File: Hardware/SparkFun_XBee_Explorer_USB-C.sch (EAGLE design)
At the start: 54 parts, among them J3 USB Female Type C Connector, J4 QWIIC_RIGHT_ANGLE, U2 AP63203, U5 ESD Diode, U7 FT231XS

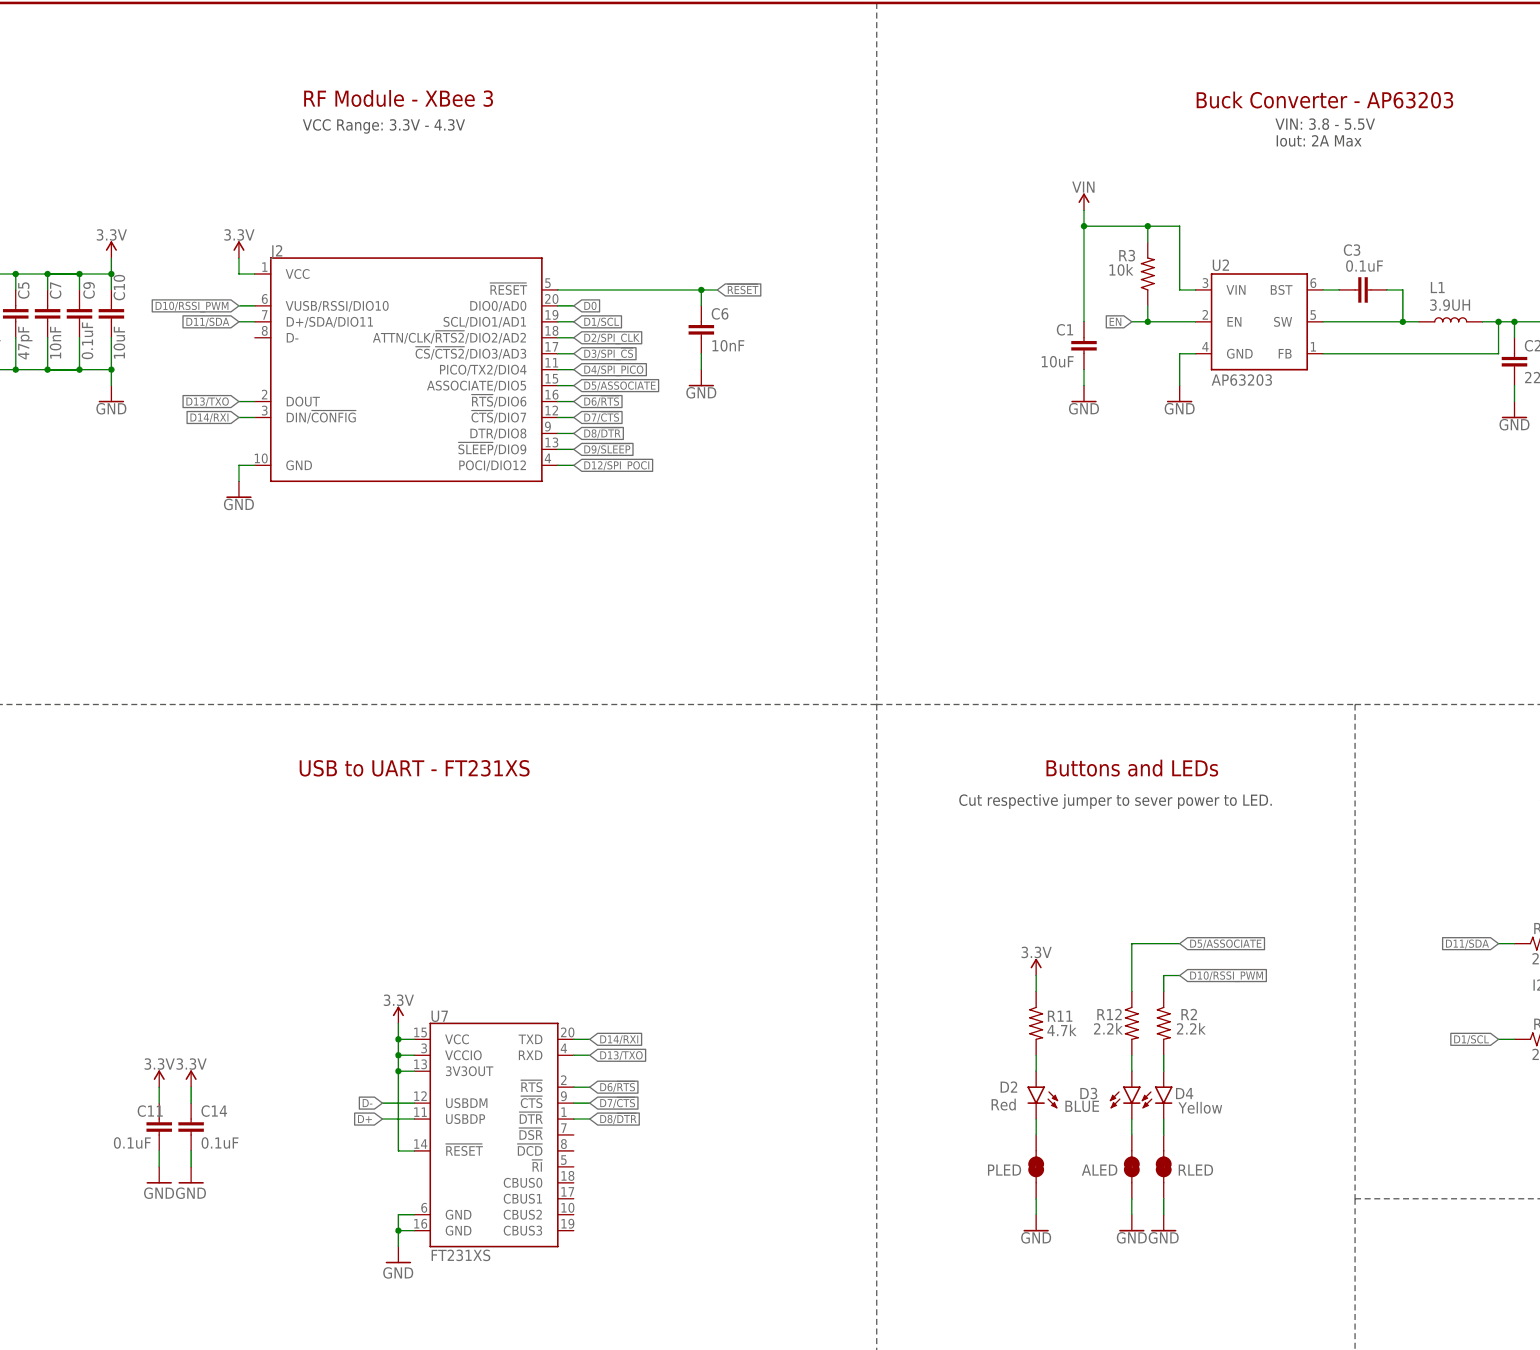
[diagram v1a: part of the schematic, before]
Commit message: Fixes anchors on some title labels in the schematic, adds more vias
* Increases the size of the Qwiic logo
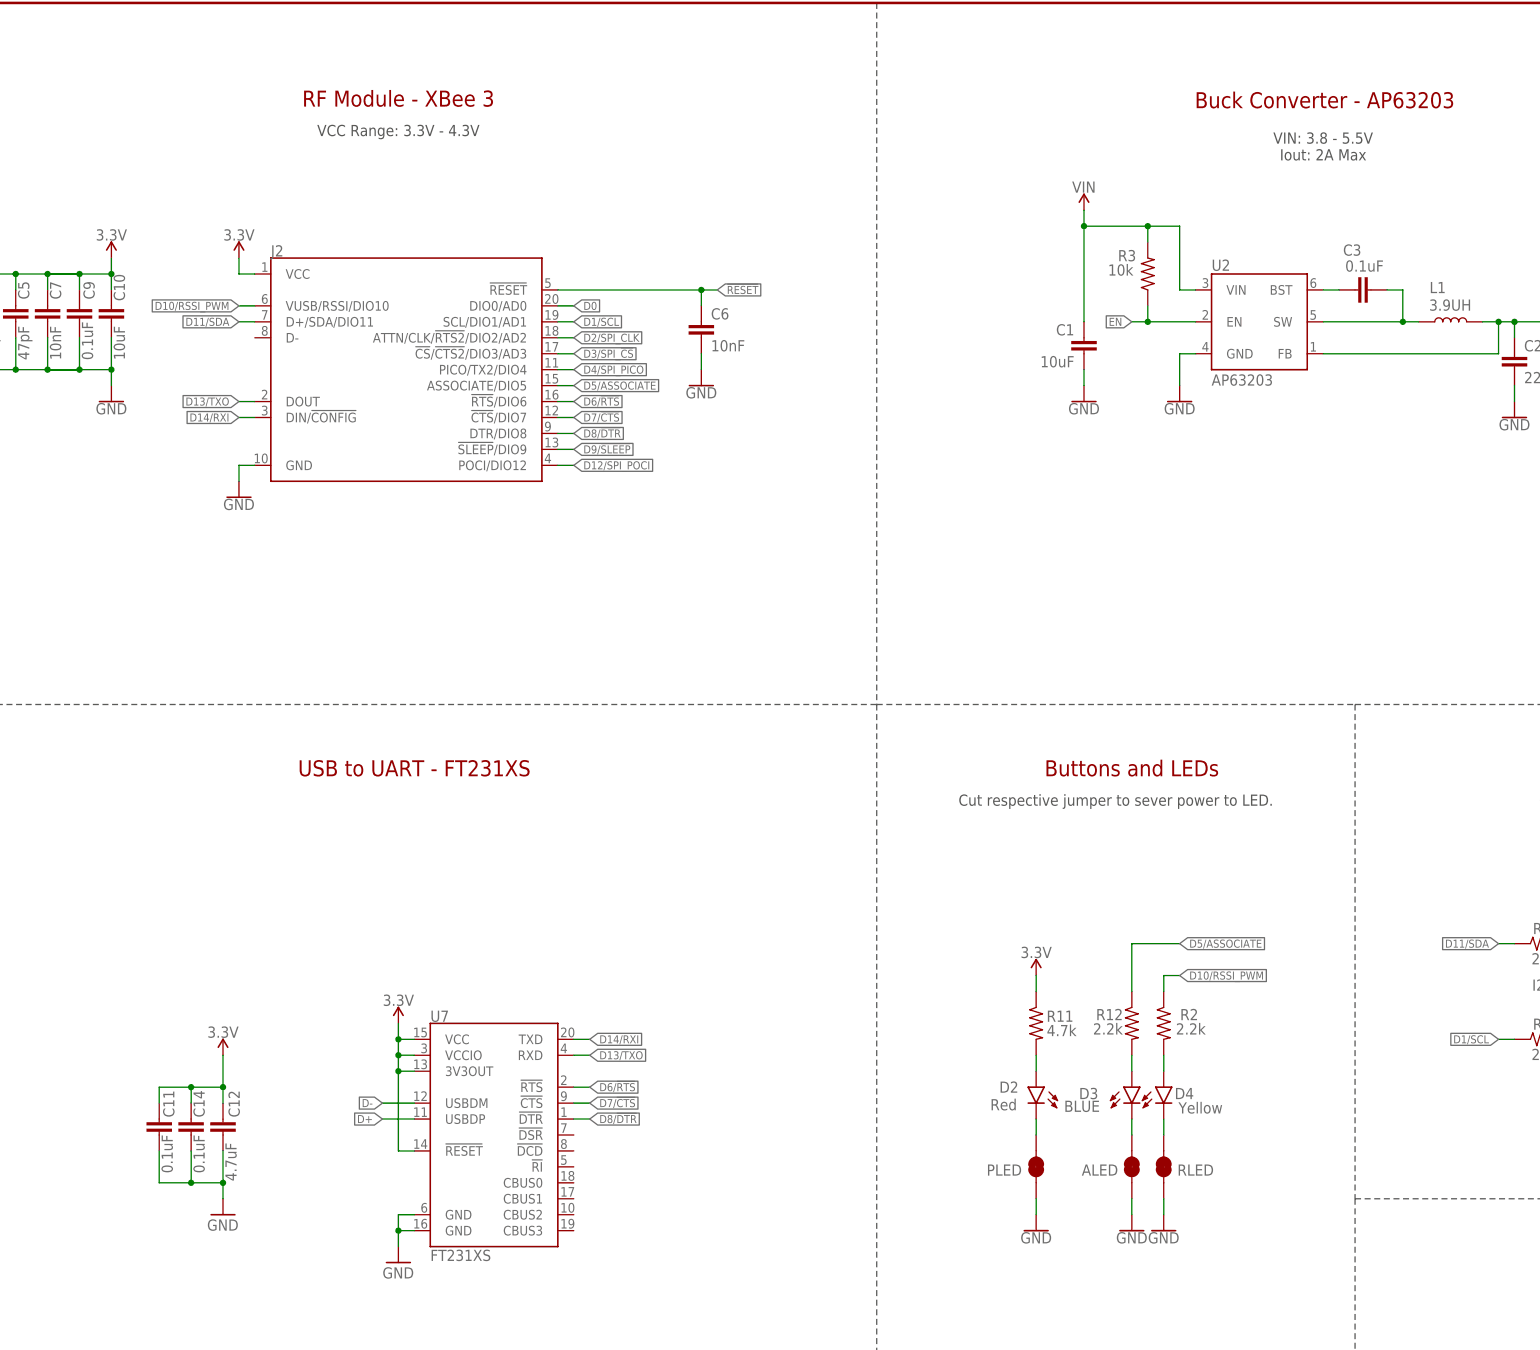
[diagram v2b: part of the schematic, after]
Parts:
- added C12: 4.7uF, SparkFun-Capacitors:4.7UF-0603-6.3V-(10%)
- LOGO3: value QWIIC_LOGO_3MM -> QWIIC_LOGO_4MM; device SparkFun-Aesthetics:QWIIC_LOGO_3MM -> SparkFun-Aesthetics:QWIIC_LOGO_4MM
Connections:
- net 3.3V: now also C12.1
- net GND: now also C12.2
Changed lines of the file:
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@@
 <part name="ALED" library="SparkFun-Jumpers" deviceset="JUMPER-SMT_2_NC_TRACE" device="_SILK" package3d_urn="urn:adsk.eagle:package:39281/1"/>
 <part name="LOGO2" library="SparkFun-Aesthetics" deviceset="OSHW-LOGO" device="S"/>
-<part name="LOGO3" library="SparkFun-Aesthetics" deviceset="QWIIC_LOGO" device="_3MM" value="QWIIC_LOGO_3MM"/>
+<part name="LOGO3" library="SparkFun-Aesthetics" deviceset="QWIIC_LOGO" device="_4MM" value="QWIIC_LOGO_4MM"/>
 <part name="U2" library="SparkFun-IC-Power" deviceset="AP63203" device="" value="AP63203"/>
 <part name="L1" library="SparkFun-Coils" deviceset="3.9UH" device="" value="3.9UH"/>
@@
 <part name="C14" library="SparkFun-Capacitors" deviceset="0.1UF" device="-0603-25V-(+80/-20%)" value="0.1uF"/>
 <part name="C11" library="SparkFun-Capacitors" deviceset="0.1UF" device="-0603-25V-(+80/-20%)" value="0.1uF"/>
-<part name="GND5" library="SparkFun-PowerSymbols" deviceset="GND" device=""/>
-<part name="SUPPLY6" library="SparkFun-PowerSymbols" deviceset="3.3V" device=""/>
-<part name="SUPPLY2" library="SparkFun-PowerSymbols" deviceset="3.3V" device=""/>
-<part name="GND8" library="SparkFun-PowerSymbols" deviceset="GND" device=""/>
 <part name="SUPPLY3" library="SparkFun-PowerSymbols" deviceset="3.3V" device=""/>
 <part name="C5" library="SparkFun-Capacitors" deviceset="47PF" device="-0603-50V-5%" value="47pF"/>
@@
 <part name="LOGO1" library="SparkFun-Aesthetics" deviceset="SFE_LOGO_NAME" device=".2_INCH"/>
 <part name="LOGO4" library="SparkFun-Aesthetics" deviceset="SPECIAL_INSTRUCTIONS" device="-ORDERING"/>
+<part name="C12" library="SparkFun-Capacitors" deviceset="4.7UF" device="-0603-6.3V-(10%)" value="4.7uF"/>
+<part name="SUPPLY12" library="SparkFun-PowerSymbols" deviceset="3.3V" device=""/>
+<part name="GND9" library="SparkFun-PowerSymbols" deviceset="GND" device=""/>
 </parts>
 <sheets>
 <sheet>
 <plain>
-<text x="60.96" y="259.08" size="1.778" layer="97" font="vector">VCC Range: 3.3V - 4.3V</text>
+<text x="76.2" y="259.08" size="1.778" layer="97" font="vector" align="center">VCC Range: 3.3V - 4.3V</text>
 <text x="223.774" y="263.906" size="2.54" layer="94" font="vector" align="center">Buck Converter - AP63203</text>
 <text x="276.86" y="157.48" size="2.54" layer="94" font="vector" align="center">Qwiic - I2C</text>
@@
 <text x="363.22" y="10.16" size="2.54" layer="94" font="vector" align="center">Elias Santistevan</text>
 <text x="193.04" y="157.48" size="2.54" layer="94" font="vector" align="center">Buttons and LEDs</text>
-<text x="215.9" y="256.54" size="1.778" layer="97" font="vector">VIN: 3.8 - 5.5V
+<text x="223.52" y="256.54" size="1.778" layer="97" font="vector" align="center">VIN: 3.8 - 5.5V
 Iout: 2A Max</text>
 <text x="276.86" y="152.4" size="1.778" layer="97" font="vector" align="center">Cut I2C jumper to remove pullups.</text>
@@
 </instance>
 <instance part="C14" gate="G$1" x="43.18" y="99.06" smashed="yes">
-<attribute name="NAME" x="44.704" y="101.981" size="1.778" layer="95" font="vector"/>
-<attribute name="VALUE" x="44.704" y="96.901" size="1.778" layer="96" font="vector"/>
+<attribute name="NAME" x="45.339" y="101.854" size="1.778" layer="95" font="vector" rot="R90"/>
+<attribute name="VALUE" x="45.339" y="92.964" size="1.778" layer="96" font="vector" rot="R90"/>
 </instance>
 <instance part="C11" gate="G$1" x="38.1" y="99.06" smashed="yes">
-<attribute name="NAME" x="34.544" y="101.981" size="1.778" layer="95" font="vector"/>
-<attribute name="VALUE" x="30.734" y="96.901" size="1.778" layer="96" font="vector"/>
-</instance>
-<instance part="GND5" gate="1" x="38.1" y="91.44" smashed="yes">
-<attribute name="VALUE" x="35.56" y="88.9" size="1.778" layer="96" font="vector"/>
-</instance>
-<instance part="SUPPLY6" gate="G$1" x="38.1" y="106.68" smashed="yes">
-<attribute name="VALUE" x="38.1" y="109.474" size="1.778" layer="96" font="vector" align="bottom-center"/>
-</instance>
-<instance part="SUPPLY2" gate="G$1" x="43.18" y="106.68" smashed="yes">
-<attribute name="VALUE" x="43.18" y="109.474" size="1.778" layer="96" font="vector" align="bottom-center"/>
-</instance>
-<instance part="GND8" gate="1" x="43.18" y="91.44" smashed="yes">
-<attribute name="VALUE" x="40.64" y="88.9" size="1.778" layer="96" font="vector"/>
+<attribute name="NAME" x="40.513" y="101.854" size="1.778" layer="95" font="vector" rot="R90"/>
+<attribute name="VALUE" x="40.259" y="92.964" size="1.778" layer="96" font="vector" rot="R90"/>
 </instance>
 <instance part="SUPPLY3" gate="G$1" x="76.2" y="116.84" smashed="yes">
@@
 <instance part="LOGO1" gate="G$1" x="330.2" y="33.02" smashed="yes"/>
 <instance part="LOGO4" gate="G$1" x="394.97" y="12.446" smashed="yes"/>
+<instance part="C12" gate="G$1" x="48.26" y="99.06" smashed="yes">
+<attribute name="NAME" x="50.927" y="101.854" size="1.778" layer="95" font="vector" rot="R90"/>
+<attribute name="VALUE" x="50.419" y="91.694" size="1.778" layer="96" font="vector" rot="R90"/>
+</instance>
+<instance part="SUPPLY12" gate="G$1" x="48.26" y="111.76" smashed="yes">
+<attribute name="VALUE" x="48.26" y="114.554" size="1.778" layer="96" font="vector" align="bottom-center"/>
+</instance>
+<instance part="GND9" gate="1" x="48.26" y="86.36" smashed="yes">
+<attribute name="VALUE" x="45.72" y="83.82" size="1.778" layer="96" font="vector"/>
+</instance>
 </instances>
 <busses>
@@
 <segment>
 <pinref part="C11" gate="G$1" pin="2"/>
-<wire x1="38.1" y1="93.98" x2="38.1" y2="96.52" width="0.1524" layer="91"/>
-<pinref part="GND5" gate="1" pin="GND"/>
-</segment>
-<segment>
+<wire x1="38.1" y1="91.44" x2="38.1" y2="96.52" width="0.1524" layer="91"/>
 <pinref part="C14" gate="G$1" pin="2"/>
-<wire x1="43.18" y1="96.52" x2="43.18" y2="93.98" width="0.1524" layer="91"/>
-<pinref part="GND8" gate="1" pin="GND"/>
+<wire x1="43.18" y1="96.52" x2="43.18" y2="91.44" width="0.1524" layer="91"/>
+<pinref part="C12" gate="G$1" pin="2"/>
+<pinref part="GND9" gate="1" pin="GND"/>
+<wire x1="48.26" y1="96.52" x2="48.26" y2="91.44" width="0.1524" layer="91"/>
+<wire x1="48.26" y1="91.44" x2="48.26" y2="88.9" width="0.1524" layer="91"/>
+<wire x1="43.18" y1="91.44" x2="48.26" y2="91.44" width="0.1524" layer="91"/>
+<junction x="43.18" y="91.44"/>
+<junction x="48.26" y="91.44"/>
+<wire x1="38.1" y1="91.44" x2="43.18" y2="91.44" width="0.1524" layer="91"/>
 </segment>
 <segment>
@@
 </segment>
 <segment>
-<pinref part="SUPPLY2" gate="G$1" pin="3.3V"/>
+<pinref part="C11" gate="G$1" pin="1"/>
+<wire x1="38.1" y1="104.14" x2="38.1" y2="106.68" width="0.1524" layer="91"/>
 <pinref part="C14" gate="G$1" pin="1"/>
 <wire x1="43.18" y1="104.14" x2="43.18" y2="106.68" width="0.1524" layer="91"/>
-</segment>
-<segment>
-<pinref part="SUPPLY6" gate="G$1" pin="3.3V"/>
-<pinref part="C11" gate="G$1" pin="1"/>
-<wire x1="38.1" y1="104.14" x2="38.1" y2="106.68" width="0.1524" layer="91"/>
-</segment>
-<segment>
+<pinref part="C12" gate="G$1" pin="1"/>
+<wire x1="48.26" y1="111.76" x2="48.26" y2="106.68" width="0.1524" layer="91"/>
+<pinref part="SUPPLY12" gate="G$1" pin="3.3V"/>
+<wire x1="48.26" y1="106.68" x2="48.26" y2="104.14" width="0.1524" layer="91"/>
+<wire x1="43.18" y1="106.68" x2="48.26" y2="106.68" width="0.1524" layer="91"/>
+<junction x="43.18" y="106.68"/>
+<junction x="48.26" y="106.68"/>
+<wire x1="38.1" y1="106.68" x2="43.18" y2="106.68" width="0.1524" layer="91"/>
+</segment>
+<segment>
